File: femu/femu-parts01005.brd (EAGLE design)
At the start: 24.1 x 15.8 mm, 54 parts, among them IC1 ESP32-QFN_5X5, IC3 FT230XQ

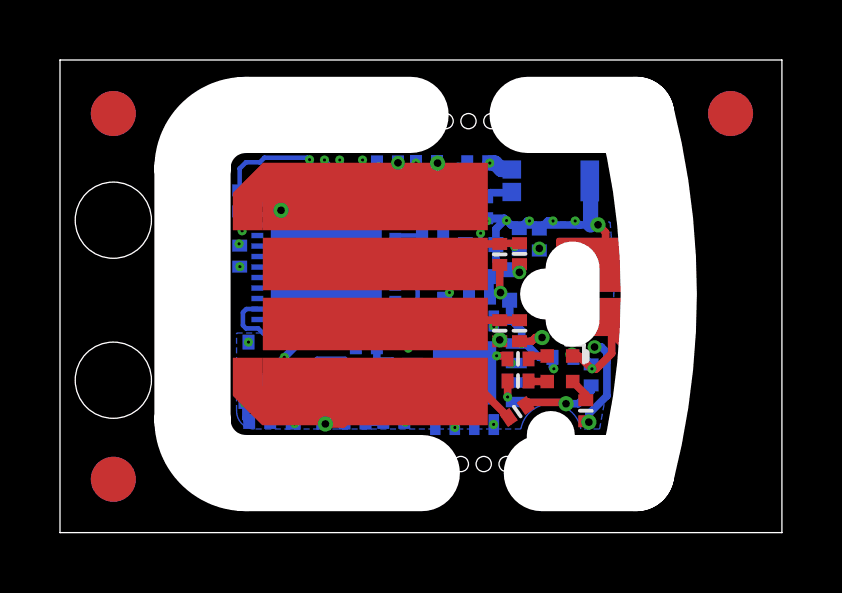
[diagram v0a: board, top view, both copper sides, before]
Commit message: Adding new 01005 parts library, and a femu board with 01005 sized passives near the edges to avoid milling issues during PCB fabrication. Removed tNames and tValues layer text of FB 1 in femu.brd. Adding PCBWay 4 layer CAM job
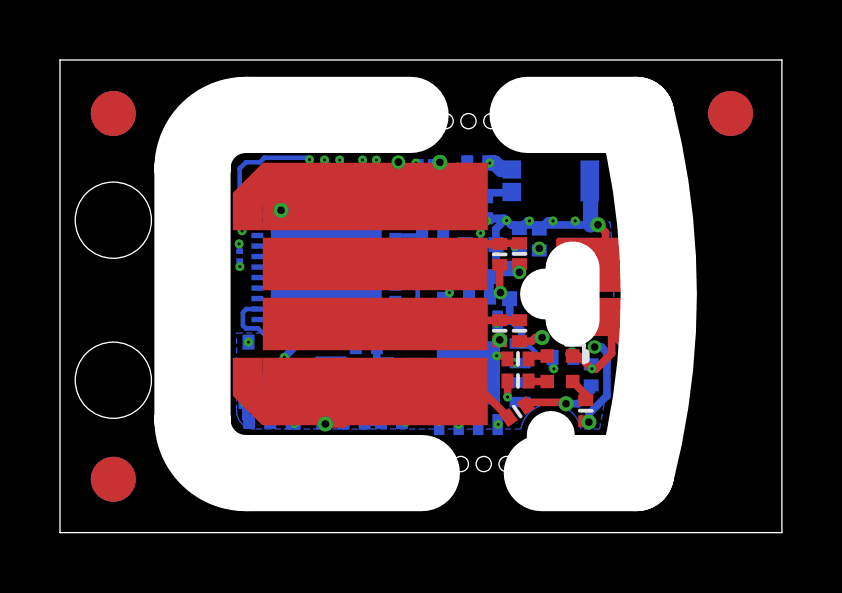
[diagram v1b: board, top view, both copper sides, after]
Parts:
- C13, C17, C20, R1: device parts_0201:PART -> parts_01005:01005
- moved C20 0.31 mm to (10.7, 12.1)
- moved IC3 0.13 mm to (13.6, 5.33)
- moved C27 0.08 mm to (11.1, 3.71)
- moved C10 0.05 mm to (15.0, 8.31)
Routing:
- net GND: track 71.7 -> 73.6 mm

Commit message: Adjusting PCBWay_4_layer.cam to have milling as a drill file, moving some passives a bit to give FTDI chip some distance from passives, updating DRC settings .dru file to have tented vias
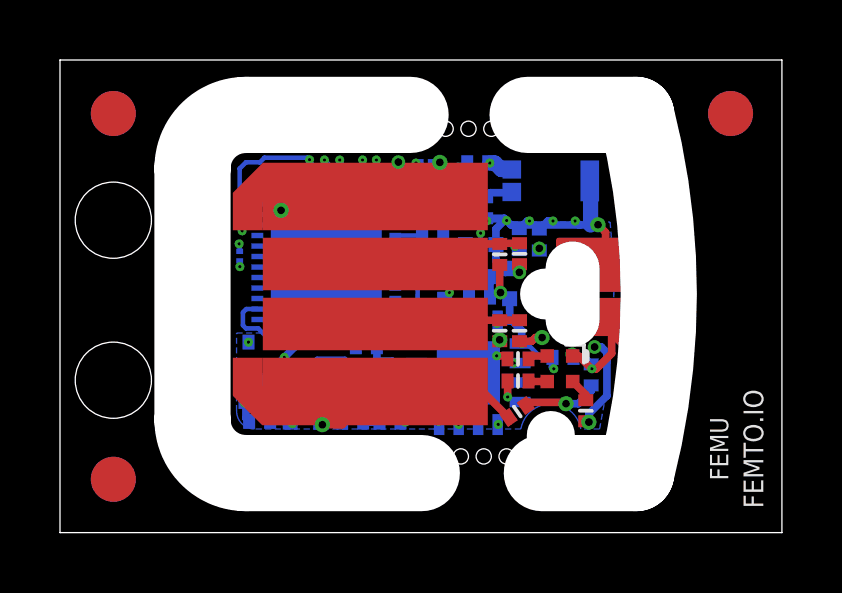
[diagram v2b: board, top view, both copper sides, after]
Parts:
- moved FB1 0.10 mm to (8.18, 3.68)
- moved C27 0.06 mm to (11.0, 3.68)
- moved C23 0.05 mm to (9.76, 3.68)
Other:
- board text added: "FEMTO.IO"
- board text added: "FEMU"
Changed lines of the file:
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@@
 <wire x1="16.361" y1="3.254" x2="16.361" y2="1.779" width="1.6" layer="46"/>
 <wire x1="19.206" y1="13.924" x2="15.586" y2="13.924" width="2.54" layer="46"/>
-<hole x="12.854" y="13.716" drill="0.508"/>
-<hole x="13.616" y="13.716" drill="0.508"/>
-<hole x="14.378" y="13.716" drill="0.508"/>
-<hole x="13.362" y="2.286" drill="0.508"/>
-<hole x="14.124" y="2.286" drill="0.508"/>
-<hole x="14.886" y="2.286" drill="0.508"/>
+<hole x="12.854" y="13.462" drill="0.508"/>
+<hole x="13.616" y="13.462" drill="0.508"/>
+<hole x="14.378" y="13.462" drill="0.508"/>
+<hole x="13.362" y="2.54" drill="0.508"/>
+<hole x="14.124" y="2.54" drill="0.508"/>
+<hole x="14.886" y="2.54" drill="0.508"/>
 <hole x="1.778" y="10.414" drill="2.54"/>
 <hole x="1.778" y="5.08" drill="2.54"/>
@@
 <vertex x="1.778" y="3.937" curve="-90"/>
 </polygon>
+<text x="23.114" y="2.794" size="0.6604" layer="25" font="vector" ratio="20" rot="R90" align="center">FEMTO.IO</text>
+<text x="21.971" y="2.794" size="0.6096" layer="25" font="vector" ratio="20" rot="R90" align="center">FEMU</text>
 </plain>
 <attributes>
@@
 </class>
 </classes>
-<designrules name="oshpark-4layer-blind-burried-vias *">
+<designrules name="oshpark-4layer-blind-burried-vias">
 <description language="en">&lt;b&gt;OSH Park Design Rules&lt;/b&gt;
 &lt;p&gt;
@@
 <param name="mlMinCreamFrame" value="0mil"/>
 <param name="mlMaxCreamFrame" value="0mil"/>
-<param name="mlViaStopLimit" value="0mil"/>
+<param name="mlViaStopLimit" value="10mil"/>
 <param name="srRoundness" value="0"/>
 <param name="srMinRoundness" value="0mil"/>
@@
 <attribute name="MPN" value="GRM033C80J104KE84D" x="15.2162" y="9.7536" size="0.5" layer="28" rot="MR270" display="off"/>
 </element>
-<element name="C27" library="parts_0201" package="PART" value="0.1uF" x="11.0506" y="3.7084" smashed="yes" rot="MR180">
-<attribute name="MPN" value="GRM033C80J104KE84D" x="11.0506" y="2.9464" size="0.5" layer="28" rot="MR180" display="off"/>
+<element name="C27" library="parts_0201" package="PART" value="0.1uF" x="10.9998" y="3.683" smashed="yes" rot="MR180">
+<attribute name="MPN" value="GRM033C80J104KE84D" x="10.9998" y="2.921" size="0.5" layer="28" rot="MR180" display="off"/>
 </element>
 <element name="U$37" library="usb-type-a-pcb-footprint-only" package="USB-A-MALE" value="USB-A-PCB" x="10.511" y="7.954" smashed="yes"/>
@@
 <attribute name="MPN" value="CC0201JRNPO8BN470" x="15.3178" y="9.294" size="0.5" layer="27" rot="R90" display="off"/>
 </element>
-<element name="FB1" library="microbuilder" package="_0402MP" value="" x="8.282" y="3.683" smashed="yes" rot="MR0">
-<attribute name="MPN" value="BLM15PD121SN1D" x="8.282" y="3.683" size="1.778" layer="28" rot="MR0" display="off"/>
-<attribute name="VALUE" x="8.917" y="2.8892" size="0.4064" layer="28" ratio="10" rot="MR0"/>
-</element>
-<element name="C23" library="parts_0201" package="PART" value="4.7uF" x="9.806" y="3.683" smashed="yes" rot="MR0">
-<attribute name="MPN" value="GRM035R60G475ME15D" x="9.806" y="3.683" size="1.778" layer="28" rot="MR0" display="off"/>
+<element name="FB1" library="microbuilder" package="_0402MP" value="" x="8.1804" y="3.683" smashed="yes" rot="MR0">
+<attribute name="MPN" value="BLM15PD121SN1D" x="8.1804" y="3.683" size="1.778" layer="28" rot="MR0" display="off"/>
+<attribute name="VALUE" x="8.8154" y="2.8892" size="0.4064" layer="28" ratio="10" rot="MR0"/>
+</element>
+<element name="C23" library="parts_0201" package="PART" value="4.7uF" x="9.7552" y="3.683" smashed="yes" rot="MR0">
+<attribute name="MPN" value="GRM035R60G475ME15D" x="9.7552" y="3.683" size="1.778" layer="28" rot="MR0" display="off"/>
 </element>
 <element name="C24" library="parts_0201" package="PART" value="10nF" x="15.2416" y="4.0386" smashed="yes" rot="R215">
@@
 <wire x1="15.9782" y1="10.1036" x2="16.2632" y2="10.3886" width="0.254" layer="16"/>
 <wire x1="16.2632" y1="10.3886" x2="16.4354" y2="10.3886" width="0.254" layer="16"/>
-<wire x1="10.156" y1="3.683" x2="10.2632" y2="3.683" width="0.254" layer="16"/>
-<wire x1="10.2632" y1="3.683" x2="10.6752" y2="3.683" width="0.254" layer="16"/>
-<wire x1="10.6752" y1="3.683" x2="10.7006" y2="3.7084" width="0.254" layer="16"/>
+<wire x1="10.1052" y1="3.683" x2="10.2632" y2="3.683" width="0.254" layer="16"/>
+<wire x1="10.2632" y1="3.683" x2="10.6498" y2="3.683" width="0.254" layer="16"/>
 <wire x1="10.511" y1="11.204" x2="7.8276" y2="11.204" width="0.1524" layer="1"/>
 <wire x1="7.8276" y1="11.204" x2="7.3676" y2="10.744" width="0.1524" layer="1"/>
@@
 <wire x1="10.1108" y1="3.8354" x2="10.2632" y2="3.683" width="0.254" layer="16"/>
 <wire x1="10.5624" y1="4.572" x2="10.5624" y2="4.253" width="0.254" layer="16"/>
-<wire x1="10.7006" y1="4.1148" x2="10.7006" y2="3.7084" width="0.254" layer="16"/>
-<wire x1="10.7006" y1="4.1148" x2="10.5624" y2="4.253" width="0.254" layer="16"/>
+<wire x1="10.6498" y1="4.1656" x2="10.6498" y2="3.683" width="0.254" layer="16"/>
+<wire x1="10.6498" y1="4.1656" x2="10.5624" y2="4.253" width="0.254" layer="16"/>
 <wire x1="11.888" y1="5.652" x2="11.33" y2="5.652" width="0.254" layer="16"/>
 <via x="11.33" y="5.652" extent="15-16" drill="0.1016" diameter="0.3048"/>
@@
 <wire x1="15.338" y1="5.652" x2="15.14" y2="5.652" width="0.254" layer="16"/>
 <contactref element="FB1" pad="2"/>
-<wire x1="7.774" y1="3.683" x2="7.8248" y2="3.6322" width="0.254" layer="16"/>
-<via x="7.8248" y="3.6322" extent="15-16" drill="0.1016" diameter="0.3048"/>
+<wire x1="7.7232" y1="3.6322" x2="7.7486" y2="3.6322" width="0.254" layer="16"/>
+<wire x1="7.7232" y1="3.6322" x2="7.6724" y2="3.683" width="0.254" layer="16"/>
+<via x="7.7486" y="3.6322" extent="15-16" drill="0.1016" diameter="0.3048"/>
 <wire x1="8.0788" y1="3.6322" x2="8.5614" y2="4.1148" width="0.254" layer="15"/>
-<wire x1="7.8248" y1="3.6322" x2="8.0788" y2="3.6322" width="0.254" layer="15"/>
+<wire x1="7.7486" y1="3.6322" x2="8.0788" y2="3.6322" width="0.254" layer="15"/>
 <contactref element="C27" pad="2"/>
 <contactref element="C23" pad="2"/>
@@
 <wire x1="11.5078" y1="3.683" x2="11.33" y2="3.5052" width="0.254" layer="15"/>
 <wire x1="11.33" y1="3.5052" x2="9.806" y2="3.5052" width="0.254" layer="15"/>
-<wire x1="11.4006" y1="3.7084" x2="11.4824" y2="3.7084" width="0.254" layer="16"/>
-<wire x1="11.4824" y1="3.7084" x2="11.5078" y2="3.683" width="0.254" layer="16"/>
+<wire x1="11.3498" y1="3.683" x2="11.5078" y2="3.683" width="0.254" layer="16"/>
 <via x="11.5078" y="3.683" extent="15-16" drill="0.1016" diameter="0.3048"/>
-<wire x1="9.456" y1="3.683" x2="9.456" y2="3.70530625" width="0.254" layer="16"/>
-<wire x1="9.456" y1="3.70530625" x2="9.5018" y2="3.75110625" width="0.254" layer="16"/>
+<wire x1="9.4052" y1="3.683" x2="9.43369375" y2="3.683" width="0.254" layer="16"/>
+<wire x1="9.43369375" y1="3.683" x2="9.5018" y2="3.75110625" width="0.254" layer="16"/>
 <via x="9.5018" y="3.75110625" extent="15-16" drill="0.1016" diameter="0.3048"/>
 <wire x1="9.552" y1="3.7592" x2="9.54390625" y2="3.75110625" width="0.254" layer="15"/>
@@
 <wire x1="7.0838" y1="4.2954" x2="7.0838" y2="3.7874" width="0.2032" layer="16"/>
 <wire x1="7.0838" y1="3.7874" x2="7.0048" y2="3.7084" width="0.254" layer="16"/>
-<wire x1="7.0048" y1="3.7084" x2="7.7486" y2="3.7084" width="0.254" layer="16"/>
-<wire x1="7.7486" y1="3.7084" x2="7.774" y2="3.683" width="0.254" layer="16"/>
+<wire x1="7.0048" y1="3.7084" x2="7.647" y2="3.7084" width="0.254" layer="16"/>
+<wire x1="7.647" y1="3.7084" x2="7.6724" y2="3.683" width="0.254" layer="16"/>
 </signal>
 <signal name="USB-">
@@
 <signal name="N$5">
 <contactref element="U$37" pad="4/VUSB"/>
-<wire x1="8.8462" y1="3.6222" x2="9.4292" y2="3.6222" width="0.254" layer="1"/>
-<wire x1="9.4292" y1="3.6222" x2="10.511" y2="4.704" width="0.254" layer="1"/>
+<wire x1="8.7446" y1="3.5968" x2="9.4038" y2="3.5968" width="0.254" layer="1"/>
+<wire x1="9.4038" y1="3.5968" x2="10.511" y2="4.704" width="0.254" layer="1"/>
 <contactref element="FB1" pad="1"/>
-<wire x1="8.8462" y1="3.6222" x2="8.8462" y2="3.6268" width="0.254" layer="16"/>
-<wire x1="8.79" y1="3.683" x2="8.8462" y2="3.6268" width="0.254" layer="16"/>
-<via x="8.8462" y="3.6222" extent="1-16" drill="0.254" diameter="0.508"/>
+<wire x1="8.7446" y1="3.5968" x2="8.7446" y2="3.6268" width="0.254" layer="16"/>
+<wire x1="8.7446" y1="3.6268" x2="8.6884" y2="3.683" width="0.254" layer="16"/>
+<via x="8.7446" y="3.5968" extent="1-16" drill="0.254" diameter="0.508"/>
 <contactref element="C24" pad="2"/>
 <wire x1="10.511" y1="4.704" x2="14.088740625" y2="4.704" width="0.254" layer="1"/>

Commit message: Minor tweaks again
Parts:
- moved C20 0.20 mm to (10.8, 12.3)
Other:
- board text added: "1.0.0"
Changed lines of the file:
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@@
 <setting verticaltext="up"/>
 </settings>
-<grid distance="1" unitdist="mil" unit="mil" style="dots" multiple="1" display="yes" altdistance="5" altunitdist="mil" altunit="mil"/>
+<grid distance="10" unitdist="mil" unit="mil" style="dots" multiple="1" display="yes" altdistance="5" altunitdist="mil" altunit="mil"/>
 <layers>
 <layer number="1" name="Top" color="4" fill="1" visible="yes" active="yes"/>
@@
 <vertex x="1.778" y="3.937" curve="-90"/>
 </polygon>
-<text x="23.114" y="2.794" size="0.6604" layer="25" font="vector" ratio="20" rot="R90" align="center">FEMTO.IO</text>
+<text x="23.114" y="4.318" size="0.6604" layer="25" font="vector" ratio="20" rot="R90" align="center">FEMTO.IO</text>
 <text x="21.971" y="2.794" size="0.6096" layer="25" font="vector" ratio="20" rot="R90" align="center">FEMU</text>
+<text x="21.971" y="5.842" size="0.6096" layer="25" font="vector" ratio="20" rot="R90" align="center">1.0.0</text>
 </plain>
 <attributes>
@@
 <attribute name="MPN" value="GRM033C80J104KE84D" x="22.9124" y="-29.3544" size="0.5" layer="28" rot="MR0" display="off"/>
 </element>
-<element name="C20" library="parts_01005" package="01005" value="10nF/6.3V(10%)" x="10.68738125" y="12.12341875" smashed="yes" rot="MR0">
-<attribute name="MPN" value="GRM022R60J103KE19L" x="29.93738125" y="-36.72658125" size="0.5" layer="28" rot="MR0" display="off"/>
+<element name="C20" library="parts_01005" package="01005" value="10nF/6.3V(10%)" x="10.81438125" y="12.27581875" smashed="yes" rot="MR0">
+<attribute name="MPN" value="GRM022R60J103KE19L" x="30.06438125" y="-36.57418125" size="0.5" layer="28" rot="MR0" display="off"/>
 </element>
 <element name="C21" library="parts_0201" package="PART" value="3.3nF/6.3V(10%)" x="12.8208" y="8.1788" smashed="yes" rot="MR270">
@@
 <wire x1="18.1864" y1="8.382" x2="18.1864" y2="10.0092" width="0.254" layer="1"/>
 <wire x1="18.1864" y1="10.0092" x2="17.934" y2="10.2616" width="0.254" layer="1"/>
-<wire x1="10.84738125" y1="12.12341875" x2="11.05058125" y2="12.12341875" width="0.1524" layer="16"/>
-<wire x1="11.05058125" y1="12.12341875" x2="11.27918125" y2="12.35201875" width="0.1524" layer="16"/>
+<wire x1="10.97438125" y1="12.27581875" x2="11.20298125" y2="12.27581875" width="0.1524" layer="16"/>
+<wire x1="11.20298125" y1="12.27581875" x2="11.27918125" y2="12.35201875" width="0.1524" layer="16"/>
 <wire x1="10.511" y1="11.204" x2="11.27918125" y2="11.97218125" width="0.254" layer="1"/>
 <wire x1="11.27918125" y1="11.97218125" x2="11.27918125" y2="12.35201875" width="0.254" layer="1"/>
@@
 <contactref element="IC1" pad="48"/>
 <contactref element="C20" pad="2"/>
-<wire x1="10.4526" y1="11.6778" x2="10.4526" y2="12.005975" width="0.1524" layer="16"/>
-<wire x1="10.4526" y1="12.005975" x2="10.52738125" y2="12.12341875" width="0.1524" layer="16"/>
+<wire x1="10.4526" y1="11.6778" x2="10.4526" y2="12.0740375" width="0.1524" layer="16"/>
+<wire x1="10.65438125" y1="12.27581875" x2="10.4526" y2="12.0740375" width="0.1524" layer="16"/>
 <wire x1="12.8208" y1="8.5288" x2="12.8208" y2="8.5774" width="0.1524" layer="16"/>
 <wire x1="12.8208" y1="8.5774" x2="12.9302" y2="8.6868" width="0.1524" layer="16"/>
 <via x="12.9302" y="8.6868" extent="15-16" drill="0.1016" diameter="0.3048"/>
-<wire x1="10.54515" y1="12.4206" x2="10.52738125" y2="12.40283125" width="0.1524" layer="16"/>
-<wire x1="10.52738125" y1="12.40283125" x2="10.52738125" y2="12.12341875" width="0.1524" layer="16"/>
+<wire x1="10.54515" y1="12.4206" x2="10.65438125" y2="12.31136875" width="0.1524" layer="16"/>
+<wire x1="10.65438125" y1="12.31136875" x2="10.65438125" y2="12.27581875" width="0.1524" layer="16"/>
 <via x="10.54515" y="12.4206" extent="15-16" drill="0.1016" diameter="0.3048"/>
 <wire x1="10.54515" y1="12.4206" x2="10.54515" y2="11.07185" width="0.254" layer="15"/>

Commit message: Updating part names, and cleaning up + filling in MPN attributes
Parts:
- renumbered U$11 to ANT1, U$33 to LDO1
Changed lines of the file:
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@@
 </element>
 <element name="C17" library="parts_01005" package="01005" value="0.1uF" x="5.9888" y="11.057" smashed="yes" rot="MR90">
-<attribute name="MPN" value=" GRM022R60G104ME15L " x="-27.4612" y="-7.843" size="0.5" layer="28" rot="MR90" display="off"/>
+<attribute name="MPN" value="GRM022R60G104ME15L" x="-27.4612" y="-7.843" size="0.5" layer="28" rot="MR90" display="off"/>
 </element>
 <element name="C18" library="parts_0201" package="PART" value="1uF" x="6.631" y="6.35" smashed="yes" rot="MR180">
@@
 <attribute name="VERSION" value="v01" x="-1.2526" y="2.9262" size="0.5" layer="27" display="off"/>
 </element>
-<element name="U$11" library="bar_antenna" package="ANT_BAR" value="PULSE_ANT_2.4GHZ" x="16.3594" y="11.724" smashed="yes" rot="MR180"/>
+<element name="ANT1" library="bar_antenna" package="ANT_BAR" value="PULSE_ANT_2.4GHZ" x="16.3594" y="11.724" smashed="yes" rot="MR180">
+<attribute name="MPN" value="W3008" x="16.3594" y="11.724" size="1.778" layer="28" rot="MR180" display="off"/>
+</element>
 <element name="FRAME3" library="SparkFun-Aesthetics" package="DUMMY" value="FRAME-LETTERNO_PACKAGE" x="-1.2886" y="1.6604" smashed="yes">
 <attribute name="DESIGNER" value="Nobody" x="-1.2886" y="1.6604" size="0.5" layer="27" display="off"/>
@@
 </element>
 <element name="U$37" library="usb-type-a-pcb-footprint-only" package="USB-A-MALE" value="USB-A-PCB" x="10.511" y="7.954" smashed="yes"/>
-<element name="IC3" library="ftdichip" library_urn="urn:adsk.eagle:library:231" package="QFN16" package3d_urn="urn:adsk.eagle:package:14017/1" value="FT230XQ" x="13.613" y="5.327" smashed="yes" rot="MR180"/>
+<element name="IC3" library="ftdichip" library_urn="urn:adsk.eagle:library:231" package="QFN16" package3d_urn="urn:adsk.eagle:package:14017/1" value="FT230XQ" x="13.613" y="5.327" smashed="yes" rot="MR180">
+<attribute name="MPN" value="FT230XQ-R" x="13.613" y="5.327" size="1.778" layer="28" rot="MR180" display="off"/>
+</element>
 <element name="R8" library="parts_0201" package="PART" value="27" x="14.6574" y="6.731" smashed="yes" rot="R270">
 <attribute name="MPN" value="ERJ-1GNF27R0C" x="14.6574" y="6.731" size="0.5" layer="27" rot="R270" display="off"/>
@@
 <element name="FID5" library="adafruit" package="FIDUCIAL_1MM" value="FIDUCIAL" x="1.778" y="13.97" smashed="yes" rot="MR0"/>
 <element name="FID6" library="adafruit" package="FIDUCIAL_1MM" value="FIDUCIAL" x="22.352" y="13.97" smashed="yes" rot="MR0"/>
-<element name="U$33" library="onsemi" package="WLCSP4" value="NCP167AFCT330T2G" x="6.9088" y="4.4704" smashed="yes" rot="MR0"/>
+<element name="LDO1" library="onsemi" package="WLCSP4" value="NCP167AFCT330T2G" x="6.9088" y="4.4704" smashed="yes" rot="MR0">
+<attribute name="MPN" value="NCP167AFCT330T2G" x="6.9088" y="4.4704" size="1.778" layer="28" rot="MR0" display="off"/>
+</element>
 <element name="C2" library="parts_0201" package="PART" value="1uF" x="6.6548" y="3.7084" smashed="yes" rot="MR180">
 <attribute name="MPN" value="CL03A105KQ3CSNH" x="6.6548" y="3.048" size="1.778" layer="28" rot="MR180" display="off"/>
@@
 <contactref element="C22" pad="1"/>
 <contactref element="R6" pad="1"/>
-<contactref element="U$11" pad="3"/>
-<contactref element="U$11" pad="2"/>
+<contactref element="ANT1" pad="3"/>
+<contactref element="ANT1" pad="2"/>
 <contactref element="C25" pad="1"/>
 <contactref element="C27" pad="1"/>
@@
 <wire x1="12.6622" y1="11.854" x2="12.6622" y2="12.3422" width="0.254" layer="15"/>
 <contactref element="C3" pad="1"/>
-<contactref element="U$33" pad="B2"/>
+<contactref element="LDO1" pad="B2"/>
 <contactref element="C2" pad="1"/>
 <wire x1="6.1976" y1="4.3236" x2="6.1976" y2="3.8156" width="0.254" layer="16"/>
@@
 <contactref element="C9" pad="2"/>
 <contactref element="R6" pad="2"/>
-<contactref element="U$11" pad="1"/>
+<contactref element="ANT1" pad="1"/>
 <wire x1="15.0364" y1="11.331" x2="14.3406" y2="11.331" width="0.254" layer="16"/>
 <wire x1="14.1882" y1="11.1786" x2="14.3406" y2="11.331" width="0.254" layer="16"/>
@@
 <wire x1="16.4608" y1="5.461" x2="16.4156" y2="5.5062" width="0.254" layer="16"/>
 <wire x1="16.4156" y1="5.5062" x2="16.4156" y2="5.842" width="0.254" layer="16"/>
-<contactref element="U$33" pad="A2"/>
+<contactref element="LDO1" pad="A2"/>
 <contactref element="C3" pad="2"/>
 <wire x1="6.7338" y1="4.6454" x2="6.7338" y2="5.09910625" width="0.2032" layer="16"/>
@@
 <wire x1="8.5614" y1="4.1148" x2="9.13810625" y2="4.1148" width="0.254" layer="15"/>
 <wire x1="9.13810625" y1="4.1148" x2="9.5018" y2="3.75110625" width="0.254" layer="15"/>
-<contactref element="U$33" pad="A1"/>
+<contactref element="LDO1" pad="A1"/>
 <contactref element="C2" pad="2"/>
-<contactref element="U$33" pad="B1"/>
+<contactref element="LDO1" pad="B1"/>
 <wire x1="7.0838" y1="4.6454" x2="7.0838" y2="4.2954" width="0.2032" layer="16"/>
 <wire x1="7.0838" y1="4.2954" x2="7.0838" y2="3.7874" width="0.2032" layer="16"/>

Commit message: XTAL should be using 10pF caps, not 8pF. Fixed
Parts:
- C4, C5: value 8pF -> 10pF
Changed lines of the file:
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@@
 <attribute name="MPN" value="FA-128 40.0000MF10Z-K3" x="-0.0916" y="-13.1108" size="0.5" layer="28" rot="MR180" display="off"/>
 </element>
-<element name="C4" library="parts_0201" package="PART" value="8pF" x="10.2124" y="5.334" smashed="yes" rot="MR0">
-<attribute name="MPN" value="GRM0335C1H8R0DA01D" x="15.9124" y="7.684" size="0.5" layer="28" rot="MR0" display="off"/>
+<element name="C4" library="parts_0201" package="PART" value="10pF" x="10.2124" y="5.334" smashed="yes" rot="MR0">
+<attribute name="MPN" value="CC0201JRNPO9BN100" x="15.9124" y="7.684" size="0.5" layer="28" rot="MR0" display="off"/>
 </element>
-<element name="C5" library="parts_0201" package="PART" value="8pF" x="10.2124" y="4.572" smashed="yes" rot="MR0">
-<attribute name="MPN" value="GRM0335C1H8R0DA01D" x="19.2124" y="4.122" size="0.5" layer="28" rot="MR0" display="off"/>
+<element name="C5" library="parts_0201" package="PART" value="10pF" x="10.2124" y="4.572" smashed="yes" rot="MR0">
+<attribute name="MPN" value="CC0201JRNPO9BN100" x="19.2124" y="4.122" size="0.5" layer="28" rot="MR0" display="off"/>
 </element>
 <element name="C7" library="parts_0201" package="PART" value="270pF" x="12.4222" y="9.398" smashed="yes" rot="MR180">
